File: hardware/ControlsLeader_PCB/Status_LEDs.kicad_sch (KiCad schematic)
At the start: 29 parts, among them J5 BPS_Fault_LED

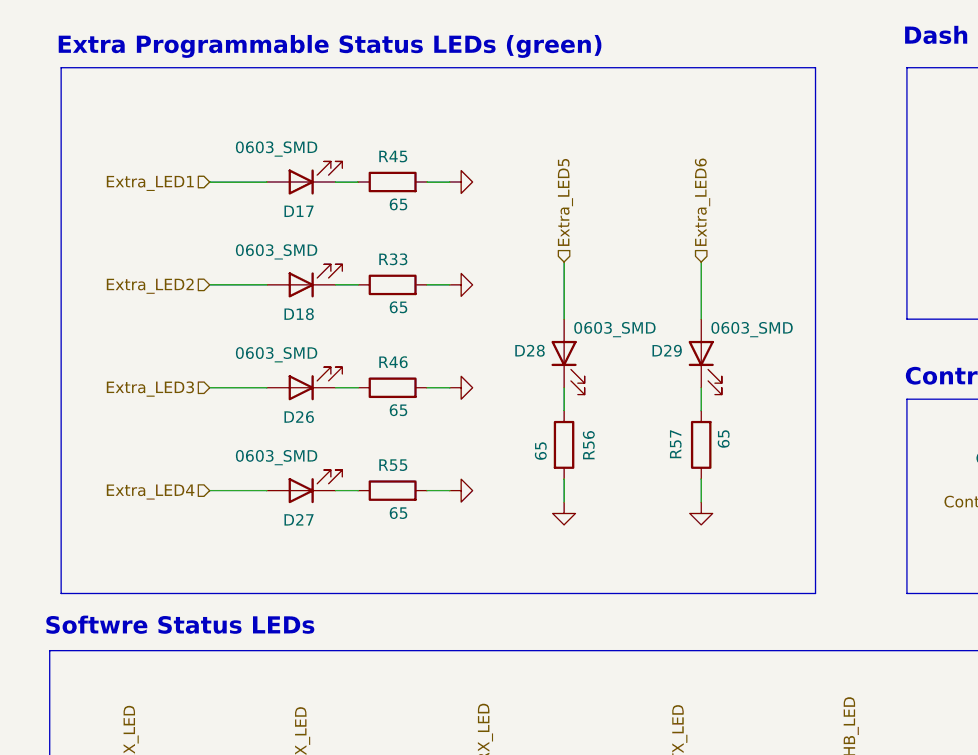
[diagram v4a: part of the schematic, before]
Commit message: Removed Extra LED 6
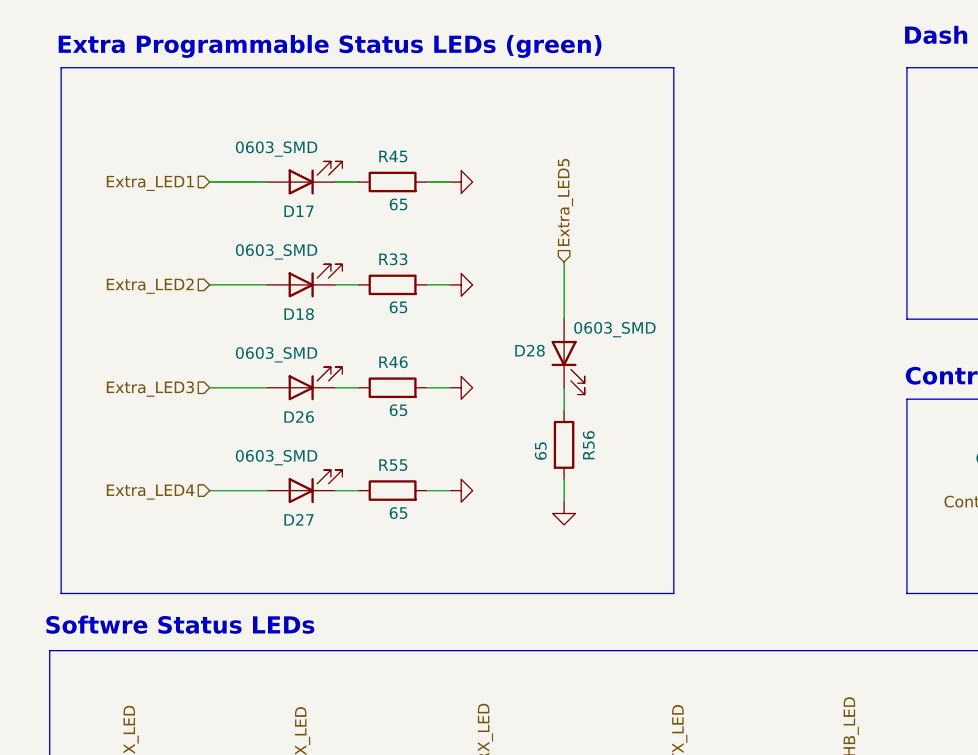
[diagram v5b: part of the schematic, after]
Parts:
- removed D29: 0603_SMD, LED_SMD:LED_0201_0603Metric_Pad0.64x0.40mm_HandSolder, symbol Device:LED
- removed R57: 65, Capacitor_SMD:C_0201_0603Metric_Pad0.64x0.40mm_HandSolder, symbol Device:R

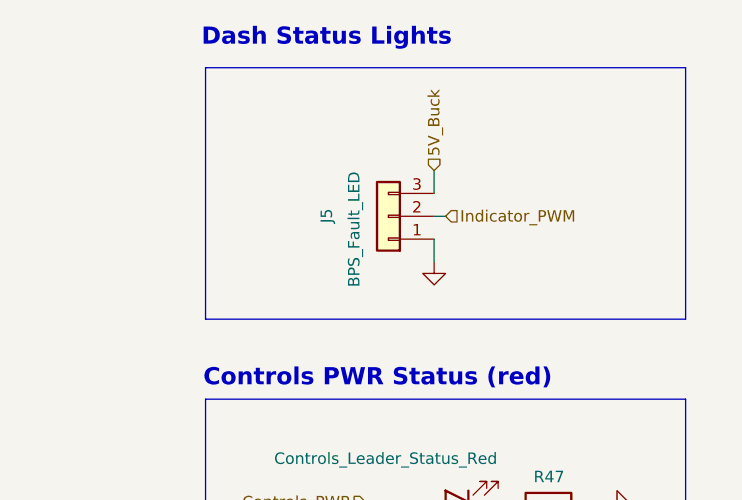
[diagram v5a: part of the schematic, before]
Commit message: Updated LSOM status LED and horn 24v signal connector layout
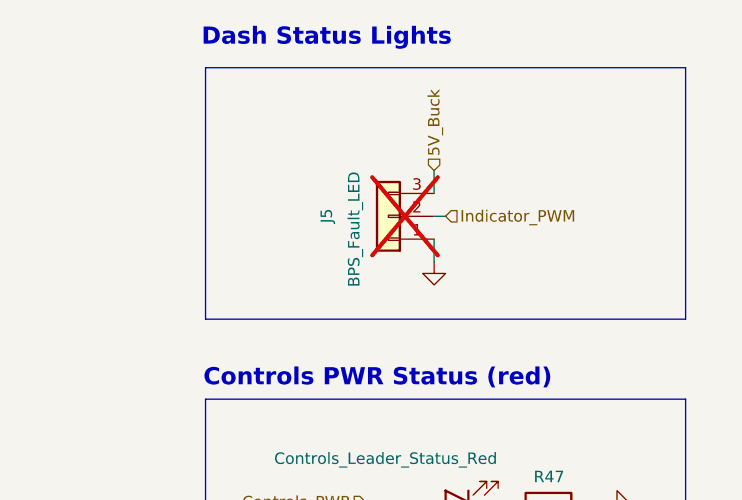
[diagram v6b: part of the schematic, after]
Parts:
- D17, D18, D19, D20, D21, D22, D23, D24, D25, D26, D27, D28: footprint LED_SMD:LED_0201_0603Metric_Pad0.64x0.40mm_HandSolder -> LED_SMD:LED_0603_1608Metric_Pad1.05x0.95mm_HandSolder
- J5: now not fitted
- R33, R45, R46, R47, R48, R49, R50, R51, R52, R53, R54, R55, R56: footprint Capacitor_SMD:C_0201_0603Metric_Pad0.64x0.40mm_HandSolder -> Capacitor_SMD:C_0603_1608Metric_Pad1.08x0.95mm_HandSolder
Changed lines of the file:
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@@
 			)
 		)
-		(property "Footprint" "LED_SMD:LED_0201_0603Metric_Pad0.64x0.40mm_HandSolder"
+		(property "Footprint" "LED_SMD:LED_0603_1608Metric_Pad1.05x0.95mm_HandSolder"
 			(at 93.98 67.31 0)
 			(effects
@@
 			)
 		)
-		(property "Footprint" "Capacitor_SMD:C_0201_0603Metric_Pad0.64x0.40mm_HandSolder"
+		(property "Footprint" "Capacitor_SMD:C_0603_1608Metric_Pad1.08x0.95mm_HandSolder"
 			(at 153.162 143.51 90)
 			(effects
@@
 			)
 		)
-		(property "Footprint" "LED_SMD:LED_0201_0603Metric_Pad0.64x0.40mm_HandSolder"
+		(property "Footprint" "LED_SMD:LED_0603_1608Metric_Pad1.05x0.95mm_HandSolder"
 			(at 205.74 129.54 0)
 			(effects
@@
 			)
 		)
-		(property "Footprint" "Capacitor_SMD:C_0201_0603Metric_Pad0.64x0.40mm_HandSolder"
+		(property "Footprint" "Capacitor_SMD:C_0603_1608Metric_Pad1.08x0.95mm_HandSolder"
 			(at 104.14 57.658 90)
 			(effects
@@
 			)
 		)
-		(property "Footprint" "Capacitor_SMD:C_0201_0603Metric_Pad0.64x0.40mm_HandSolder"
+		(property "Footprint" "Capacitor_SMD:C_0603_1608Metric_Pad1.08x0.95mm_HandSolder"
 			(at 121.412 85.09 90)
 			(effects
@@
 			)
 		)
-		(property "Footprint" "LED_SMD:LED_0201_0603Metric_Pad0.64x0.40mm_HandSolder"
+		(property "Footprint" "LED_SMD:LED_0603_1608Metric_Pad1.05x0.95mm_HandSolder"
 			(at 114.3 133.35 0)
 			(effects
@@
 			)
 		)
-		(property "Footprint" "LED_SMD:LED_0201_0603Metric_Pad0.64x0.40mm_HandSolder"
+		(property "Footprint" "LED_SMD:LED_0603_1608Metric_Pad1.05x0.95mm_HandSolder"
 			(at 135.89 133.35 0)
 			(effects
@@
 			)
 		)
-		(property "Footprint" "LED_SMD:LED_0201_0603Metric_Pad0.64x0.40mm_HandSolder"
+		(property "Footprint" "LED_SMD:LED_0603_1608Metric_Pad1.05x0.95mm_HandSolder"
 			(at 123.19 74.93 0)
 			(effects
@@
 			)
 		)
-		(property "Footprint" "Capacitor_SMD:C_0201_0603Metric_Pad0.64x0.40mm_HandSolder"
+		(property "Footprint" "Capacitor_SMD:C_0603_1608Metric_Pad1.08x0.95mm_HandSolder"
 			(at 112.522 143.51 90)
 			(effects
@@
 			)
 		)
-		(property "Footprint" "LED_SMD:LED_0201_0603Metric_Pad0.64x0.40mm_HandSolder"
+		(property "Footprint" "LED_SMD:LED_0603_1608Metric_Pad1.05x0.95mm_HandSolder"
 			(at 74.93 133.35 0)
 			(effects
@@
 			)
 		)
-		(property "Footprint" "Capacitor_SMD:C_0201_0603Metric_Pad0.64x0.40mm_HandSolder"
+		(property "Footprint" "Capacitor_SMD:C_0603_1608Metric_Pad1.08x0.95mm_HandSolder"
 			(at 104.14 91.948 90)
 			(effects
@@
 			)
 		)
-		(property "Footprint" "Capacitor_SMD:C_0201_0603Metric_Pad0.64x0.40mm_HandSolder"
+		(property "Footprint" "Capacitor_SMD:C_0603_1608Metric_Pad1.08x0.95mm_HandSolder"
 			(at 134.112 143.51 90)
 			(effects
@@
 			)
 		)
-		(property "Footprint" "LED_SMD:LED_0201_0603Metric_Pad0.64x0.40mm_HandSolder"
+		(property "Footprint" "LED_SMD:LED_0603_1608Metric_Pad1.05x0.95mm_HandSolder"
 			(at 93.98 133.35 0)
 			(effects
@@
 			)
 		)
-		(property "Footprint" "Capacitor_SMD:C_0201_0603Metric_Pad0.64x0.40mm_HandSolder"
+		(property "Footprint" "Capacitor_SMD:C_0603_1608Metric_Pad1.08x0.95mm_HandSolder"
 			(at 92.202 143.51 90)
 			(effects
@@
 			)
 		)
-		(property "Footprint" "LED_SMD:LED_0201_0603Metric_Pad0.64x0.40mm_HandSolder"
+		(property "Footprint" "LED_SMD:LED_0603_1608Metric_Pad1.05x0.95mm_HandSolder"
 			(at 175.26 133.35 0)
 			(effects
@@
 			)
 		)
-		(property "Footprint" "Capacitor_SMD:C_0201_0603Metric_Pad0.64x0.40mm_HandSolder"
+		(property "Footprint" "Capacitor_SMD:C_0603_1608Metric_Pad1.08x0.95mm_HandSolder"
 			(at 199.39 93.218 90)
 			(effects
@@
 			)
 		)
-		(property "Footprint" "Capacitor_SMD:C_0201_0603Metric_Pad0.64x0.40mm_HandSolder"
+		(property "Footprint" "Capacitor_SMD:C_0603_1608Metric_Pad1.08x0.95mm_HandSolder"
 			(at 104.14 80.518 90)
 			(effects
@@
 			)
 		)
-		(property "Footprint" "Capacitor_SMD:C_0201_0603Metric_Pad0.64x0.40mm_HandSolder"
+		(property "Footprint" "Capacitor_SMD:C_0603_1608Metric_Pad1.08x0.95mm_HandSolder"
 			(at 104.14 69.088 90)
 			(effects
@@
 			)
 		)
-		(property "Footprint" "LED_SMD:LED_0201_0603Metric_Pad0.64x0.40mm_HandSolder"
+		(property "Footprint" "LED_SMD:LED_0603_1608Metric_Pad1.05x0.95mm_HandSolder"
 			(at 154.94 133.35 0)
 			(effects
@@
 			)
 		)
-		(property "Footprint" "LED_SMD:LED_0201_0603Metric_Pad0.64x0.40mm_HandSolder"
+		(property "Footprint" "LED_SMD:LED_0603_1608Metric_Pad1.05x0.95mm_HandSolder"
 			(at 93.98 78.74 0)
 			(effects
@@
 			)
 		)
-		(property "Footprint" "Capacitor_SMD:C_0201_0603Metric_Pad0.64x0.40mm_HandSolder"
+		(property "Footprint" "Capacitor_SMD:C_0603_1608Metric_Pad1.08x0.95mm_HandSolder"
 			(at 173.482 143.51 90)
 			(effects
@@
 			)
 		)
-		(property "Footprint" "LED_SMD:LED_0201_0603Metric_Pad0.64x0.40mm_HandSolder"
+		(property "Footprint" "LED_SMD:LED_0603_1608Metric_Pad1.05x0.95mm_HandSolder"
 			(at 93.98 90.17 0)
 			(effects
@@
 			)
 		)
-		(property "Footprint" "LED_SMD:LED_0201_0603Metric_Pad0.64x0.40mm_HandSolder"
+		(property "Footprint" "LED_SMD:LED_0603_1608Metric_Pad1.05x0.95mm_HandSolder"
 			(at 93.98 55.88 0)
 			(effects
@@
 			)
 		)
-		(property "Footprint" "Capacitor_SMD:C_0201_0603Metric_Pad0.64x0.40mm_HandSolder"
+		(property "Footprint" "Capacitor_SMD:C_0603_1608Metric_Pad1.08x0.95mm_HandSolder"
 			(at 203.962 139.7 90)
 			(effects
@@
 			)
 		)
-		(property "Footprint" "Capacitor_SMD:C_0201_0603Metric_Pad0.64x0.40mm_HandSolder"
+		(property "Footprint" "Capacitor_SMD:C_0603_1608Metric_Pad1.08x0.95mm_HandSolder"
 			(at 73.152 143.51 90)
 			(effects
@@
 		(exclude_from_sim no)
 		(in_bom yes)
-		(on_board yes)
-		(dnp no)
+		(on_board no)
+		(dnp yes)
 		(property "Reference" "J5"
 			(at 174.752 60.452 90)

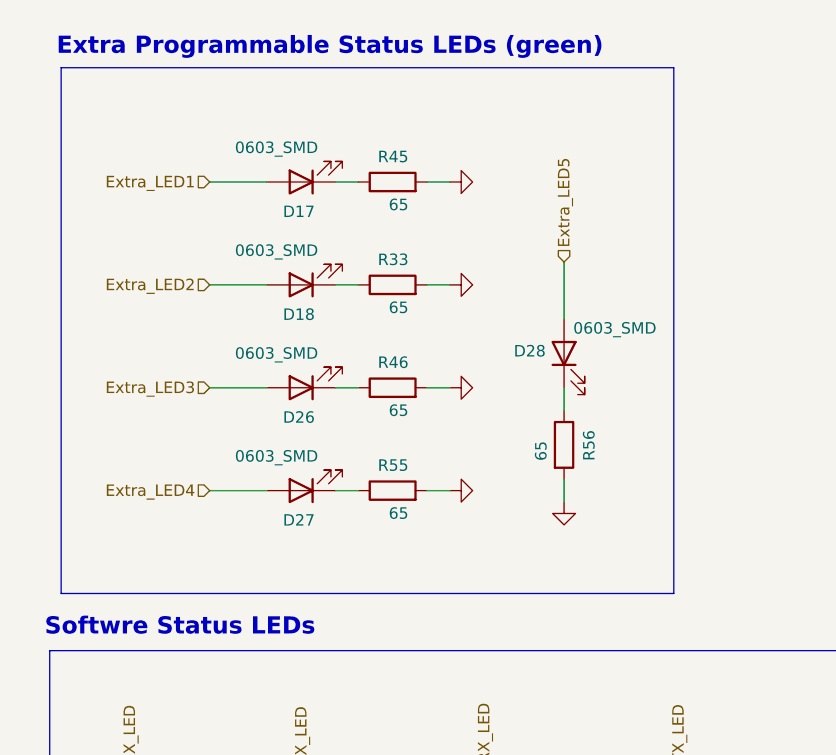
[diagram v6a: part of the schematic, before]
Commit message: PCB DESIGN DONE - need to add datasheets and p/n
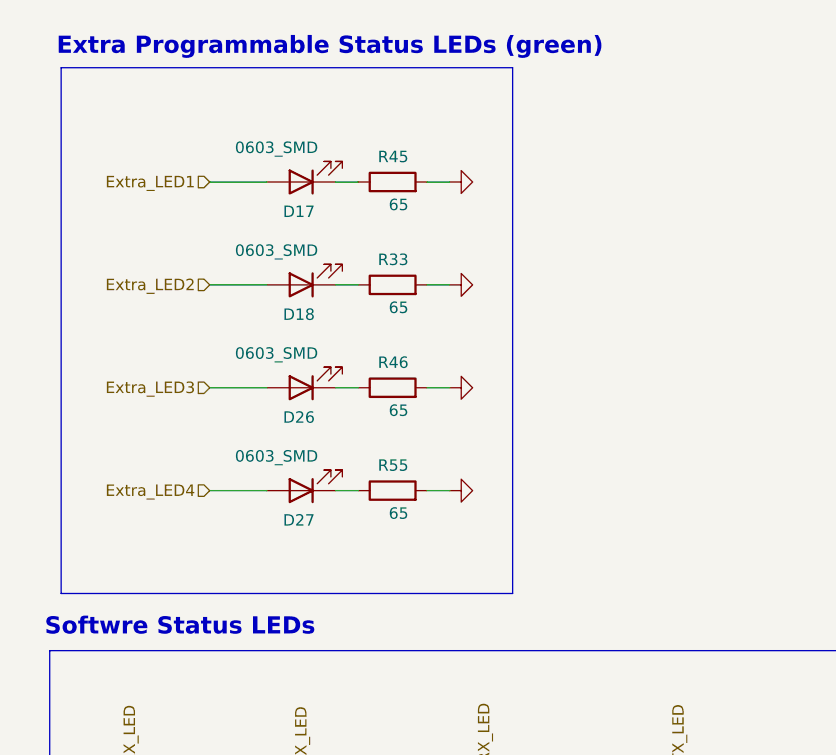
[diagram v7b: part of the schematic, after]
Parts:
- removed D28: 0603_SMD, LED_SMD:LED_0603_1608Metric_Pad1.05x0.95mm_HandSolder, symbol Device:LED
- removed R56: 65, Capacitor_SMD:C_0603_1608Metric_Pad1.08x0.95mm_HandSolder, symbol Device:R
- D16: footprint LED_SMD:LED_0201_0603Metric_Pad0.64x0.40mm_HandSolder -> LED_SMD:LED_0603_1608Metric_Pad1.05x0.95mm_HandSolder

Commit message: BOM!
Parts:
- D16: P/N (none) -> LS Q976.01-N1Q2-1-20-R18
- D17, D18, D19, D20, D21, D22, D23, D24, D25, D26, D27: P/N (none) -> LG Q976.01-MGNI-35-1
- J5: P/N 43650-0300 -> (none); now left out of the parts list
- R33, R45, R46, R55: footprint Capacitor_SMD:C_0603_1608Metric_Pad1.08x0.95mm_HandSolder -> Resistor_SMD:R_0603_1608Metric_Pad0.98x0.95mm_HandSolder; P/N (none) -> FC0402E65R0BGT0
- R47: footprint Capacitor_SMD:C_0603_1608Metric_Pad1.08x0.95mm_HandSolder -> Resistor_SMD:R_0603_1608Metric_Pad0.98x0.95mm_HandSolder; P/N (none) -> CRCW12101K10FKEAHP
- R48, R49, R50, R51, R52, R53, R54: footprint Capacitor_SMD:C_0603_1608Metric_Pad1.08x0.95mm_HandSolder -> Resistor_SMD:R_0603_1608Metric_Pad0.98x0.95mm_HandSolder; P/N (none) -> ERJ-UP6D20R0V
